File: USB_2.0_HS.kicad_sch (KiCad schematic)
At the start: 0 parts

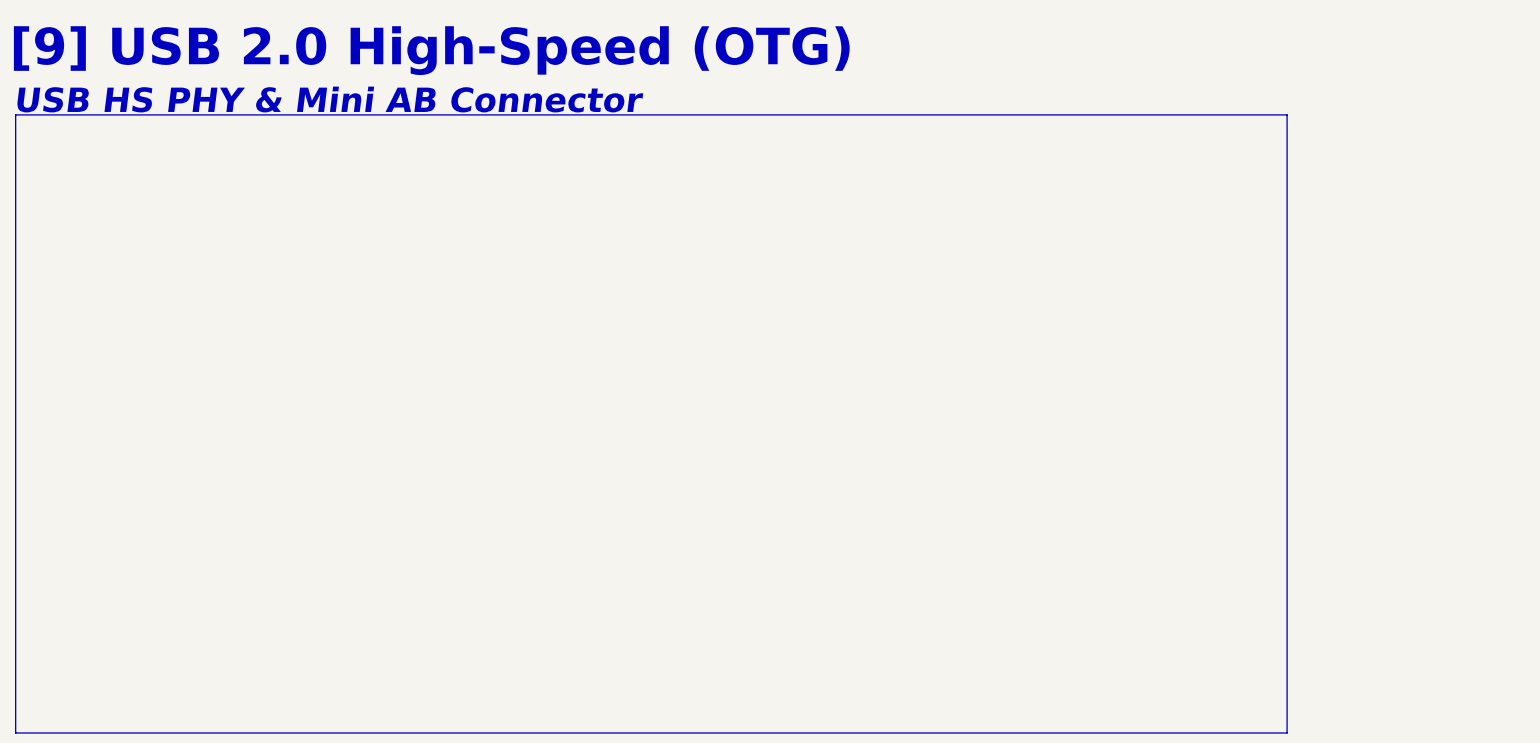
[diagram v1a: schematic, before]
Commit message: started page 9, USB2.0 hub
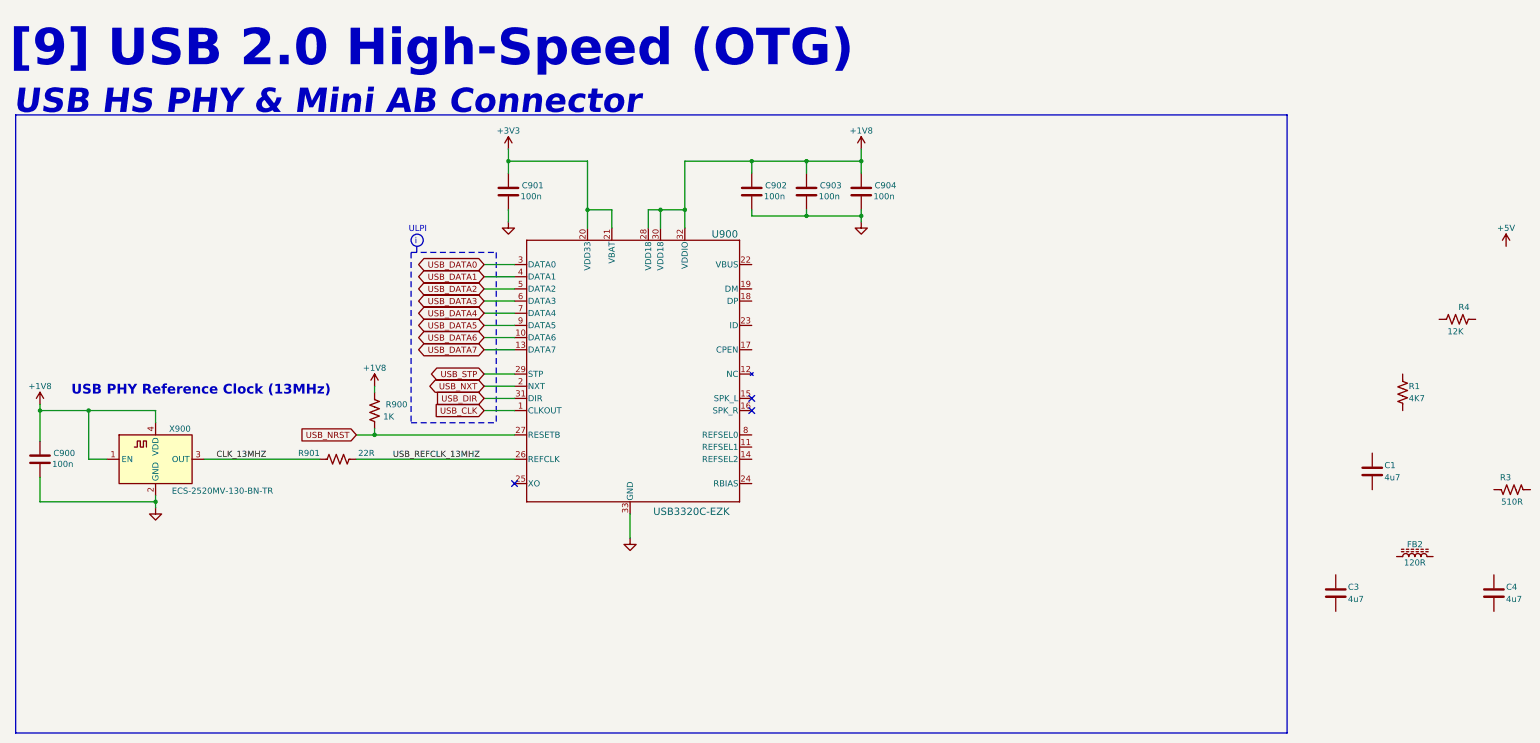
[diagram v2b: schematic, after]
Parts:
- added C1, C3, C4: 4u7, Capacitor_SMD:C_0402_1005Metric, symbol Device:C
- added C900, C901, C902, C903, C904: 100n, Capacitor_SMD:C_0402_1005Metric, symbol Device:C
- added FB2: 120R, Inductor_SMD:L_0402_1005Metric, symbol Device:L_Ferrite
- added R1: 4K7, Resistor_SMD:R_0402_1005Metric, symbol Device:R_US
- added R3: 510R, Resistor_SMD:R_0402_1005Metric, symbol Device:R_US
- added R4: 12K, Resistor_SMD:R_0402_1005Metric, symbol Device:R_US
- added R900: 1K, Resistor_SMD:R_0402_1005Metric, symbol Device:R_US
- added R901: 22R, Resistor_SMD:R_0402_1005Metric, symbol Device:R_US
- added U900: USB3320C-EZK, ZeBra_footprints:QFN32_5X5MC_MCH, symbol ZeBra-X:USB3320C-EZK
- added X900: ECS-2520MV-130-BN-TR, Oscillator:Oscillator_SMD_ECS_2520MV-xxx-xx-4Pin_2.5x2.0mm, symbol ZeBra-X:ECS-2520MV-130-BN-TR
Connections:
- new net +1V8: C900.1, C902.1, C903.1, C904.1, R900.2, U900.28 (VDD18), U900.30 (VDD18), U900.32 (VDDIO), X900.1 (EN), X900.4 (VDD)
- new net +3V3: C901.1, U900.20 (VDD33), U900.21 (VBAT)
- new net CLK_13MHZ: R901.1, X900.3 (OUT)
- new net GND: C900.2, C901.2, C902.2, C903.2, C904.2, U900.33 (GND), X900.2 (GND)
- new net USB_CLK: U900.1 (CLKOUT)
- new net USB_DATA0: U900.3 (DATA0)
- new net USB_DATA1: U900.4 (DATA1)
- new net USB_DATA2: U900.5 (DATA2)
- new net USB_DATA3: U900.6 (DATA3)
- new net USB_DATA4: U900.7 (DATA4)
- new net USB_DATA5: U900.9 (DATA5)
- new net USB_DATA6: U900.10 (DATA6)
- new net USB_DATA7: U900.13 (DATA7)
- new net USB_DIR: U900.31 (DIR)
- new net USB_NRST: R900.1, U900.27 (RESETB)
- new net USB_NXT: U900.2 (NXT)
- new net USB_REFCLK_13MHZ: R901.2, U900.26 (REFCLK)
- new net USB_STP: U900.29 (STP)
- no-connect marks 0 -> 3
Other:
- note added: "ULPI"
- note added: "USB PHY Reference Clock (13MHz)"
- note added: "i"

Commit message: finished page 9, USB 2.0 Hub
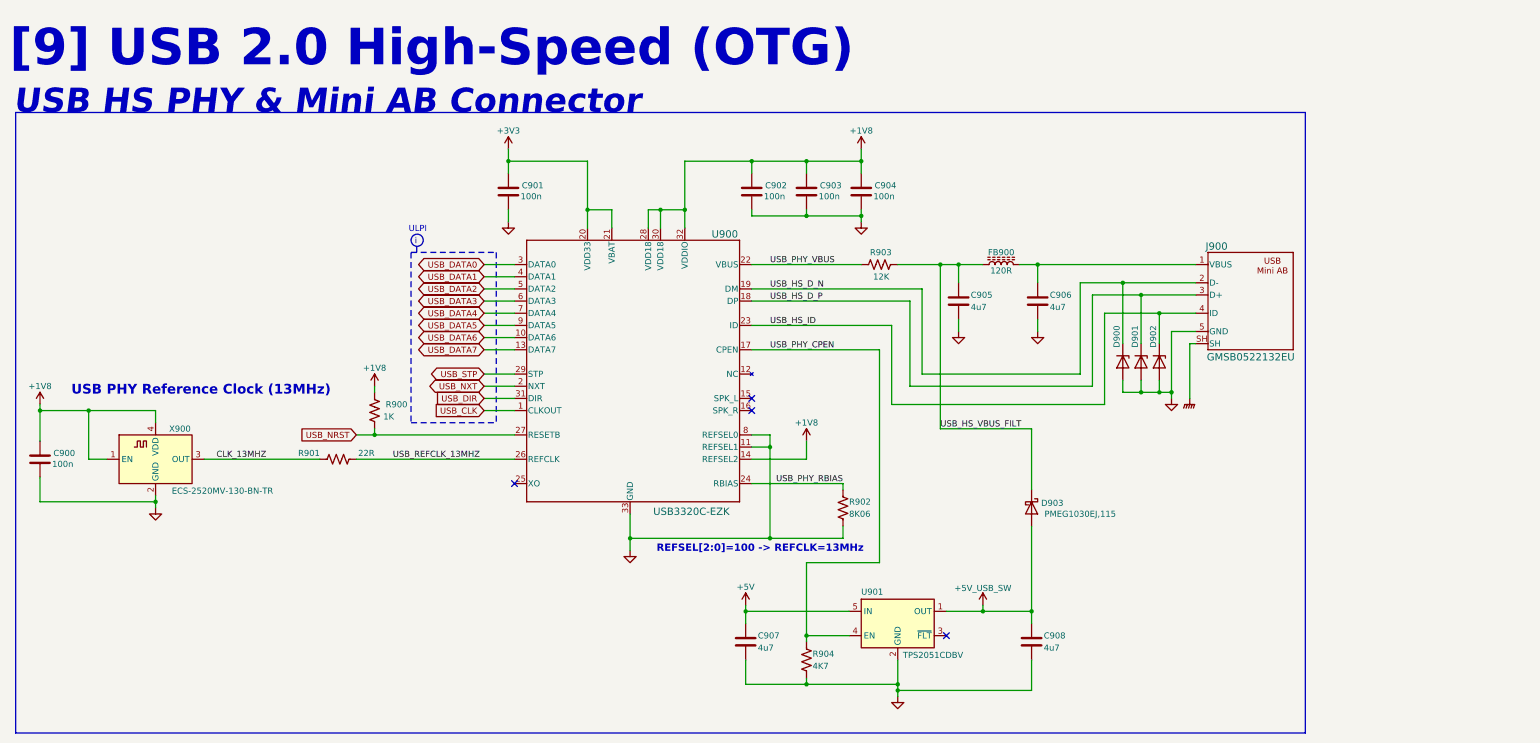
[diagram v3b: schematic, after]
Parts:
- removed R3: 510R, Resistor_SMD:R_0402_1005Metric, symbol Device:R_US
- added C907: 4u7, Capacitor_SMD:C_0402_1005Metric, symbol Device:C
- added D900, D901, D902: CG0402MLU-3.3G, Diode_SMD:D_0402_1005Metric, symbol Device:D_Zener
- added D903: PMEG1030EJ,115, Diode_SMD:D_SOD-323F, symbol Diode:PMEG1030EJ
- added J900: GMSB0522132EU, ZeBra_footprints:GMSB0522132EU, symbol ZeBra-X:GMSB0522132EU
- added R902: 8K06, Resistor_SMD:R_0402_1005Metric, symbol Device:R_US
- added U901: TPS2051CDBV, Package_TO_SOT_SMD:SOT-23-5, symbol Power_Management:TPS2051CDBV
- renumbered C3 to C905, C4 to C906, C1 to C908, FB2 to FB900, R4 to R903, R1 to R904
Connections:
- net +1V8: now also U900.14 (REFSEL2)
- net +5V: now also C907.1, U901.5 (IN)
- net GND: now also C905.2, C906.2, C908.2, R904.2, U900.11 (REFSEL1), U900.8 (REFSEL0), C907.2, D900.2 (A), D901.2 (A), D902.2 (A), J900.5 (GND), R902.2, U901.2 (GND)
- net USB_PHY_VBUS: now reaches R903.1
- net USB_PHY_VBUS: now also U900.22 (VBUS)
- net USB_HS_VBUS_FILT: now reaches R903.2
- net USB_HS_VBUS_FILT: now also C905.1, FB900.1, D903.1 (K)
- net at FB900.2: now also C906.1, J900.1 (VBUS)
- net +5V_USB_SW: now reaches C908.1
- net +5V_USB_SW: now also D903.2 (A), U901.1 (OUT)
- net USB_PHY_CPEN: now reaches U900.17 (CPEN)
- net USB_PHY_CPEN: now also R904.1, U901.4 (EN)
- net USB_HS_D_P: now reaches U900.18 (DP)
- net USB_HS_D_P: now also D901.1 (K), J900.3 (D+)
- net USB_HS_D_N: now reaches U900.19 (DM)
- net USB_HS_D_N: now also D900.1 (K), J900.2 (D-)
- net USB_HS_ID: now reaches U900.23 (ID)
- net USB_HS_ID: now also D902.1 (K), J900.4 (ID)
- net USB_PHY_RBIAS: now reaches U900.24 (RBIAS)
- net USB_PHY_RBIAS: now also R902.1
- new net GNDPWR: J900.SH
- no-connect marks 3 -> 4
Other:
- note added: "REFSEL[2:0]=100 -> REFCLK=13MHz"
- moved on the sheet: C905, C906, C908, FB900, R903, R904
